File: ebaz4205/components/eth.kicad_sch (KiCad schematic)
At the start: 4 parts

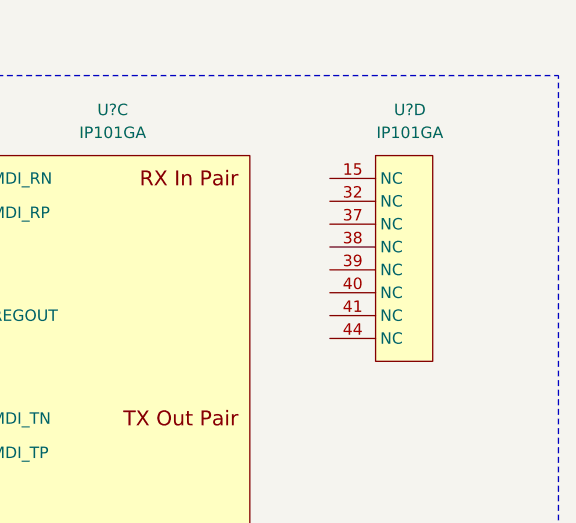
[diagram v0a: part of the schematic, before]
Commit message: Added netlist - SchComponent pin checking. Fixed symbols.
Rebuilt Xilinx symbol without bundling.
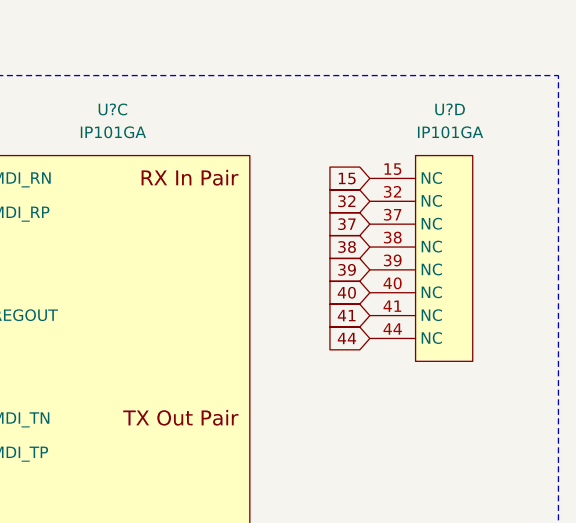
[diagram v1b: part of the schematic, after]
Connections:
- net 15: now reaches U?.15 (NC)
- net 32: now reaches U?.32 (NC)
- net 37: now reaches U?.37 (NC)
- net 38: now reaches U?.38 (NC)
- net 39: now reaches U?.39 (NC)
- net 40: now reaches U?.40 (NC)
- net 41: now reaches U?.41 (NC)
- net 44: now reaches U?.44 (NC)
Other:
- moved on the sheet: U?D
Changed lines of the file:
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@@
     (effects (font (size 1.27 1.27)) (justify right))
   )
-  (symbol (lib_id "eth:IP101GA") (at 193.04 45.72 0) (unit 4)
+  (global_label "15" (shape input) (at 188.595 11.43 180)    (property "Intersheet References" "${INTERSHEET_REFS}" (id 0) (at 182.2389 11.3506 0)
+      (effects (font (size 1.27 1.27)) (justify right) hide)
+    )
+    (effects (font (size 1.27 1.27)) (justify right))
+  )
+  (global_label "32" (shape input) (at 188.595 13.97 180)    (property "Intersheet References" "${INTERSHEET_REFS}" (id 0) (at 182.2389 13.8906 0)
+      (effects (font (size 1.27 1.27)) (justify right) hide)
+    )
+    (effects (font (size 1.27 1.27)) (justify right))
+  )
+  (global_label "37" (shape input) (at 188.595 16.51 180)    (property "Intersheet References" "${INTERSHEET_REFS}" (id 0) (at 182.2389 16.4306 0)
+      (effects (font (size 1.27 1.27)) (justify right) hide)
+    )
+    (effects (font (size 1.27 1.27)) (justify right))
+  )
+  (global_label "38" (shape input) (at 188.595 19.05 180)    (property "Intersheet References" "${INTERSHEET_REFS}" (id 0) (at 182.2389 18.9706 0)
+      (effects (font (size 1.27 1.27)) (justify right) hide)
+    )
+    (effects (font (size 1.27 1.27)) (justify right))
+  )
+  (global_label "39" (shape input) (at 188.595 21.59 180)    (property "Intersheet References" "${INTERSHEET_REFS}" (id 0) (at 182.2389 21.5106 0)
+      (effects (font (size 1.27 1.27)) (justify right) hide)
+    )
+    (effects (font (size 1.27 1.27)) (justify right))
+  )
+  (global_label "40" (shape input) (at 188.595 24.13 180)    (property "Intersheet References" "${INTERSHEET_REFS}" (id 0) (at 182.2389 24.0506 0)
+      (effects (font (size 1.27 1.27)) (justify right) hide)
+    )
+    (effects (font (size 1.27 1.27)) (justify right))
+  )
+  (global_label "41" (shape input) (at 188.595 26.67 180)    (property "Intersheet References" "${INTERSHEET_REFS}" (id 0) (at 182.2389 26.5906 0)
+      (effects (font (size 1.27 1.27)) (justify right) hide)
+    )
+    (effects (font (size 1.27 1.27)) (justify right))
+  )
+  (global_label "44" (shape input) (at 188.595 29.21 180)    (property "Intersheet References" "${INTERSHEET_REFS}" (id 0) (at 182.2389 29.1306 0)
+      (effects (font (size 1.27 1.27)) (justify right) hide)
+    )
+    (effects (font (size 1.27 1.27)) (justify right))
+  )
+  (symbol (lib_id "eth:IP101GA") (at 197.485 45.72 0) (unit 4)
     (in_bom yes) (on_board yes)
-    (property "Reference" "U?" (id 0) (at 193.04 3.81 0))
-    (property "Value" "IP101GA" (id 1) (at 193.04 6.35 0))
-    (property "Footprint" "" (id 2) (at 182.88 57.15 0)
+    (property "Reference" "U?" (id 0) (at 197.485 3.81 0))
+    (property "Value" "IP101GA" (id 1) (at 197.485 6.35 0))
+    (property "Footprint" "" (id 2) (at 187.325 57.15 0)
       (effects (font (size 1.27 1.27)) hide)
     )
-    (property "Datasheet" "" (id 3) (at 182.88 57.15 0)
+    (property "Datasheet" "" (id 3) (at 187.325 57.15 0)
       (effects (font (size 1.27 1.27)) hide)
     )

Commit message: Consolidated all custom symbols into single library.
Library is available at ebaz4205/components/ebaz4205.kicad_sym

The templates and the schematics have been updated to use this library.
Keeping the original libraries for future reference.
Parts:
- removed U? (x4): IP101GA, symbol eth:IP101GA
- added U? (x4): IP101GA, symbol ebaz4205:IP101GA
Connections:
- net 1: now also U?.1 (COL/RMII)
- net 10: now also U?.10 (LED1/PHY_AD1)
- net 11: now also U?.11 (DGND)
- net 12: now also U?.12 (LED2/PHY_AD2)
- net 13: now also U?.13 (LED3/PHY_AD3)
- net 14: now also U?.14 (VDDIO)
- net 15: now also U?.15 (NC)
- net 16: now also U?.16 (RXCLK/50M_CLKO)
- net 17: now also U?.17 (DGND)
- net 18: now also U?.18 (RXD3)
- net 19: now also U?.19 (RXD2)
- net 2: now also U?.2 (TXEN)
- net 20: now also U?.20 (RXD1)
- net 21: now also U?.21 (RXD0)
- net 22: now also U?.22 (RXDV/CRS_DV/FX_HEN)
- net 23: now also U?.23 (CRS/LEDMOD)
- net 24: now also U?.24 (RXER)
- net 25: now also U?.25 (MDC)
- net 26: now also U?.26 (MDIO)
- net 27: now also U?.27 (TEST_ON)
- net 28: now also U?.28 (ISET)
- net 29: now also U?.29 (AGND1V)
- net 3: now also U?.3 (TXD3)
- net 30: now also U?.30 (MDI_RN)
- net 31: now also U?.31 (MDI_RP)
- net 32: now also U?.32 (NC)
- net 33: now also U?.33 (MDI_TN)
- net 34: now also U?.34 (MDI_TP)
- net 35: now also U?.35 (AGND33)
- net 36: now also U?.36 (AVDD33)
- net 37: now also U?.37 (NC)
- net 38: now also U?.38 (NC)
- net 39: now also U?.39 (NC)
- net 4: now also U?.4 (TXD2)
- net 40: now also U?.40 (NC)
- net 41: now also U?.41 (NC)
- net 42: now also U?.42 (~RESET_N)
- net 43: now also U?.43 (TXER/FXSD)
- net 44: now also U?.44 (NC)
- net 45: now also U?.45 (DGND)
- net 46: now also U?.46 (X1)
- net 47: now also U?.47 (X2)
- net 48: now also U?.48 (INTR)
- net 5: now also U?.5 (TXD1)
- net 6: now also U?.6 (TXD0)
- net 7: now also U?.7 (TXCLK/50M_CLKI)
- net 8: now also U?.8 (REGOUT)
- net 9: now also U?.9 (LED0/PHY_AD0)
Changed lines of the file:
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@@
     (effects (font (size 1.27 1.27)) (justify right))
   )
-  (symbol (lib_id "eth:IP101GA") (at 197.485 45.72 0) (unit 4)
+  (symbol (lib_id "ebaz4205:IP101GA") (at 197.485 45.72 0) (unit 4)
     (in_bom yes) (on_board yes)
     (property "Reference" "U?" (id 0) (at 197.485 3.81 0))
@@
     )
   )
-  (symbol (lib_id "eth:IP101GA") (at 41.91 45.72 0) (unit 1)
+  (symbol (lib_id "ebaz4205:IP101GA") (at 41.91 45.72 0) (unit 1)
     (in_bom yes) (on_board yes)
     (property "Reference" "U?" (id 0) (at 41.91 3.81 0))
@@
     )
   )
-  (symbol (lib_id "eth:IP101GA") (at 160.02 45.72 0) (unit 3)
+  (symbol (lib_id "ebaz4205:IP101GA") (at 160.02 45.72 0) (unit 3)
     (in_bom yes) (on_board yes)
     (property "Reference" "U?" (id 0) (at 160.02 3.81 0))
@@
     )
   )
-  (symbol (lib_id "eth:IP101GA") (at 101.6 45.72 0) (unit 2)
+  (symbol (lib_id "ebaz4205:IP101GA") (at 101.6 45.72 0) (unit 2)
     (in_bom yes) (on_board yes)
     (property "Reference" "U?" (id 0) (at 101.6 3.81 0))
@@
   )
   (symbol_instances
-    (path "/c73b3085-2e42-4502-99e3-6187a3c2457b"
+    (path "/a53c8fe3-4578-4a53-8b1e-b1b1f435d0aa"
       (reference "U?") (unit 1) (value "IP101GA") (footprint "")
     )
-    (path "/65acbd75-c6b9-463e-a866-b9732c654e48"
+    (path "/27849163-fd74-406d-b632-9e067de50650"
       (reference "U?") (unit 2) (value "IP101GA") (footprint "")
     )
-    (path "/8ad766b4-df3a-4a94-9274-63fd2886fd87"
+    (path "/5e12ad9d-c6b7-429b-82d5-7a7c30328013"
       (reference "U?") (unit 3) (value "IP101GA") (footprint "")
     )
-    (path "/6af855aa-bc7c-45af-ab81-310b5b40c11f"
+    (path "/edf1c410-9a90-4563-9174-fa9b01cfd231"
       (reference "U?") (unit 4) (value "IP101GA") (footprint "")
     )
